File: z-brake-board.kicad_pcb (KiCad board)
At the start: 2 copper layers, 58 x 41 mm, 18 parts, among them J1 to Control Cabinet, J2 to Z Servo, Q2 BTS4142N, U1 LTV-817S, U2 LTV-817S, U3 LTV-817S

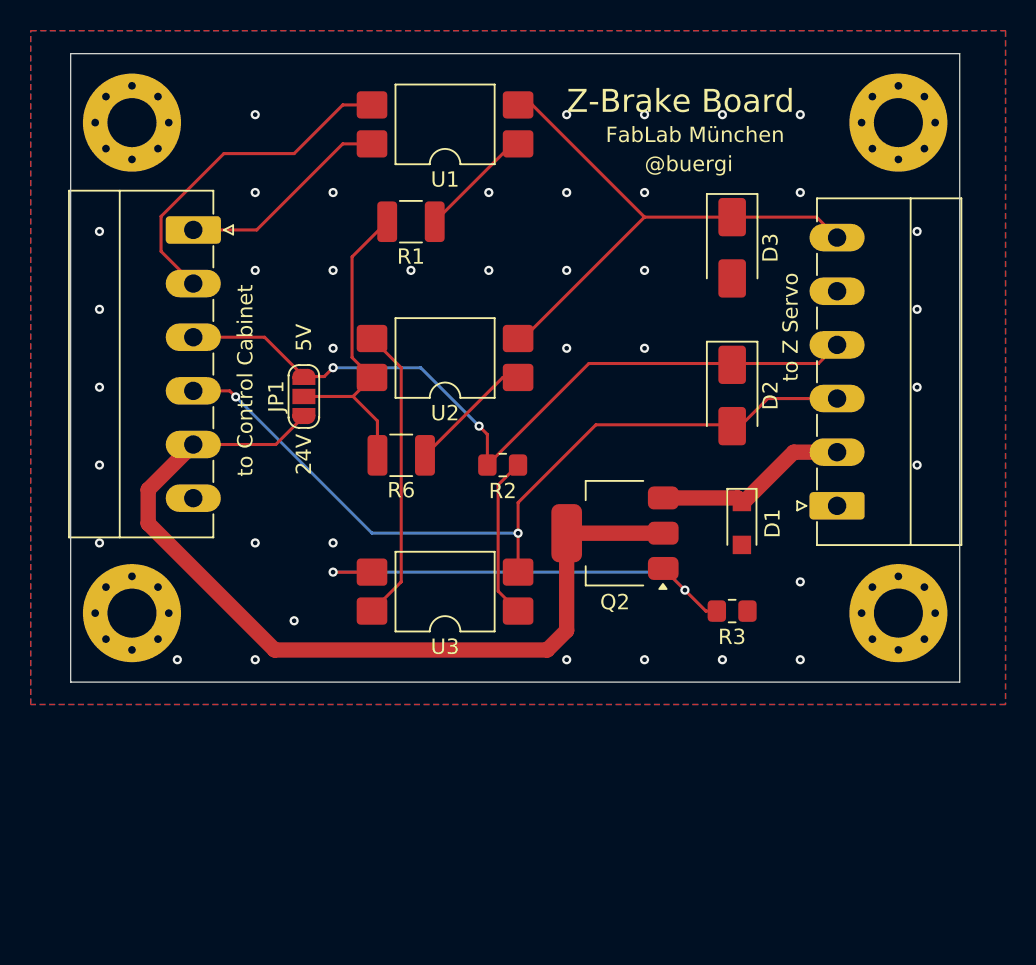
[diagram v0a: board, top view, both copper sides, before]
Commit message: Reworked design (less fancy)
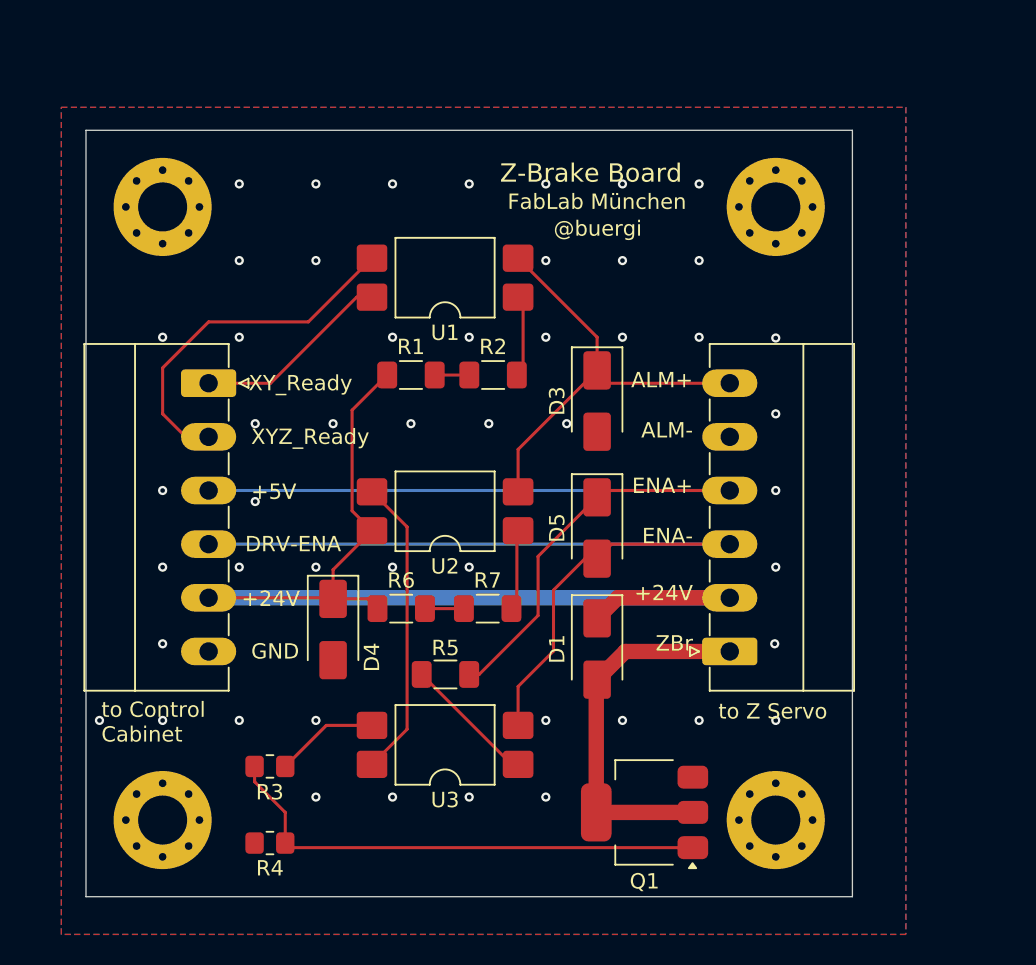
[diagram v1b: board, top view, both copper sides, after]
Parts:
- removed D2: SMAJ24A, Diode_SMD:D_SMA
- removed JP1: VCC Select, Jumper:SolderJumper-3_P1.3mm_Open_RoundedPad1.0x1.5mm_NumberLabels
- removed Q2: BTS4142N, Package_TO_SOT_SMD:SOT-223
- added D4: SMAJ24A, Diode_SMD:D_SMA, F.Cu at (71.1, 64.1)
- added D5: SMAJ5.0A, Diode_SMD:D_SMA, F.Cu at (88.3, 57.4)
- added Q1: IRFL024NPBF, Package_TO_SOT_SMD:SOT-223-3_TabPin2, F.Cu at (91.4, 76.0)
- added R4: 10k, Resistor_SMD:R_0805_2012Metric_Pad1.20x1.40mm_HandSolder, F.Cu at (67.0, 78.0)
- added R5: 2.2k, Resistor_SMD:R_1206_3216Metric_Pad1.30x1.75mm_HandSolder, F.Cu at (78.5, 67.0)
- added R7: 1k, Resistor_SMD:R_1206_3216Metric_Pad1.30x1.75mm_HandSolder, F.Cu at (81.2, 62.7)
- D1: value PMEG6020ER -> US1M; footprint Diode_SMD:Nexperia_CFP3_SOD-123W -> Diode_SMD:D_SMA
- J1: value to Control Cabinet -> Phoenix_MC_1,5_6-G-3.5
- J2: value to Z Servo -> Phoenix_MC_1,5_6-G-3.5
- R1, R6: footprint Resistor_SMD:R_1210_3225Metric_Pad1.30x2.65mm_HandSolder -> Resistor_SMD:R_1206_3216Metric_Pad1.30x1.75mm_HandSolder
- R2: value 220 -> 1k; footprint Resistor_SMD:R_0805_2012Metric_Pad1.20x1.40mm_HandSolder -> Resistor_SMD:R_1206_3216Metric_Pad1.30x1.75mm_HandSolder
- moved R3 31.8 mm to (67.0, 73.0)
- moved H4 15.7 mm to (100.0, 76.5)
- moved H3 13.6 mm to (60.0, 76.5)
- moved D3 13.3 mm to (88.3, 49.2)
- moved D1 12.5 mm to (88.3, 65.3)
- moved J2 11.8 mm to (97.0, 65.5)
- moved J1 10.0 mm to (63.0, 48.0)
- moved U1 10.0 mm to (78.4, 41.1)
- moved R1 10.0 mm to (76.2, 47.5)
- moved R6 10.0 mm to (75.6, 62.7)
- moved U2 10.0 mm to (78.4, 56.4)
- moved U3 10.0 mm to (78.4, 71.6)
- moved H2 9.71 mm to (100.0, 36.5)
- moved R2 5.91 mm to (81.6, 47.5)
- moved H1 5.85 mm to (60.0, 36.5)
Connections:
- D1 pad 1: /~{ZBrake} -> +24V
- D1 pad 2: GND -> /~{ZBrake}
- J1 pad 3: +5V -> /+5V
- J2 pad 1: GND -> /~{ZBrake}
- J2 pad 2: /~{ZBrake} -> +24V
- J2 pad 4: +5V -> /+5V
- R1 pad 1: VCC -> +24V
- R2 pad 1: +5V -> Net-(R1-Pad2)
- R3 pad 1: Net-(Q2-G) -> Net-(Q1-G)
- R3 pad 2: GND -> Net-(R3-Pad2)
- R6 pad 1: VCC -> +24V
- U1 pad 1: Net-(R1-Pad2) -> Net-(R2-Pad2)
- U2 pad 1: Net-(R6-Pad2) -> Net-(R7-Pad2)
- U2 pad 4: VCC -> +24V
- U3 pad 1: Net-(R2-Pad2) -> Net-(R5-Pad2)
- U3 pad 3: Net-(Q2-G) -> Net-(R3-Pad2)
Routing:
- net /+5V: track 0.00 -> 58.4 mm
- net +5V: track 50.3 -> 0.00 mm, vias 2 -> 0
- net Net-(Q1-G): track 0.00 -> 32.5 mm
- net Net-(Q2-G): track 30.6 -> 0.00 mm, vias 2 -> 0
- net VCC: track 21.1 -> 0.00 mm
- net +24V: track 58.3 -> 71.7 mm
- net /~{ZBrake}: track 12.8 -> 24.4 mm
- net Net-(R5-Pad2): track 0.00 -> 8.72 mm
- net /ALM+: track 35.9 -> 28.5 mm
- net Net-(R3-Pad2): track 0.00 -> 6.77 mm
- net Net-(R6-Pad2): track 8.18 -> 2.54 mm
- net Net-(R2-Pad2): track 10.6 -> 5.22 mm
- net Net-(R1-Pad2): track 7.54 -> 2.26 mm
- net Net-(R7-Pad2): track 0.00 -> 5.11 mm
- net /DRV-ENA-5V: track 53.2 -> 57.3 mm, vias 2 -> 0
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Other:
- board size 58 x 41 mm -> 50 x 50 mm
- board text added: "+24V"
- board text added: "+5V"
- board text added: "ALM+"
- board text added: "ALM-"
- board text added: "DRV-ENA"
- board text added: "ENA+"
- board text added: "ENA-"
- board text added: "GND"
- board text added: "XYZ_Ready"
- board text added: "XY_Ready"
- board text added: "ZBr"

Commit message: Shrunk board to 48x48mm
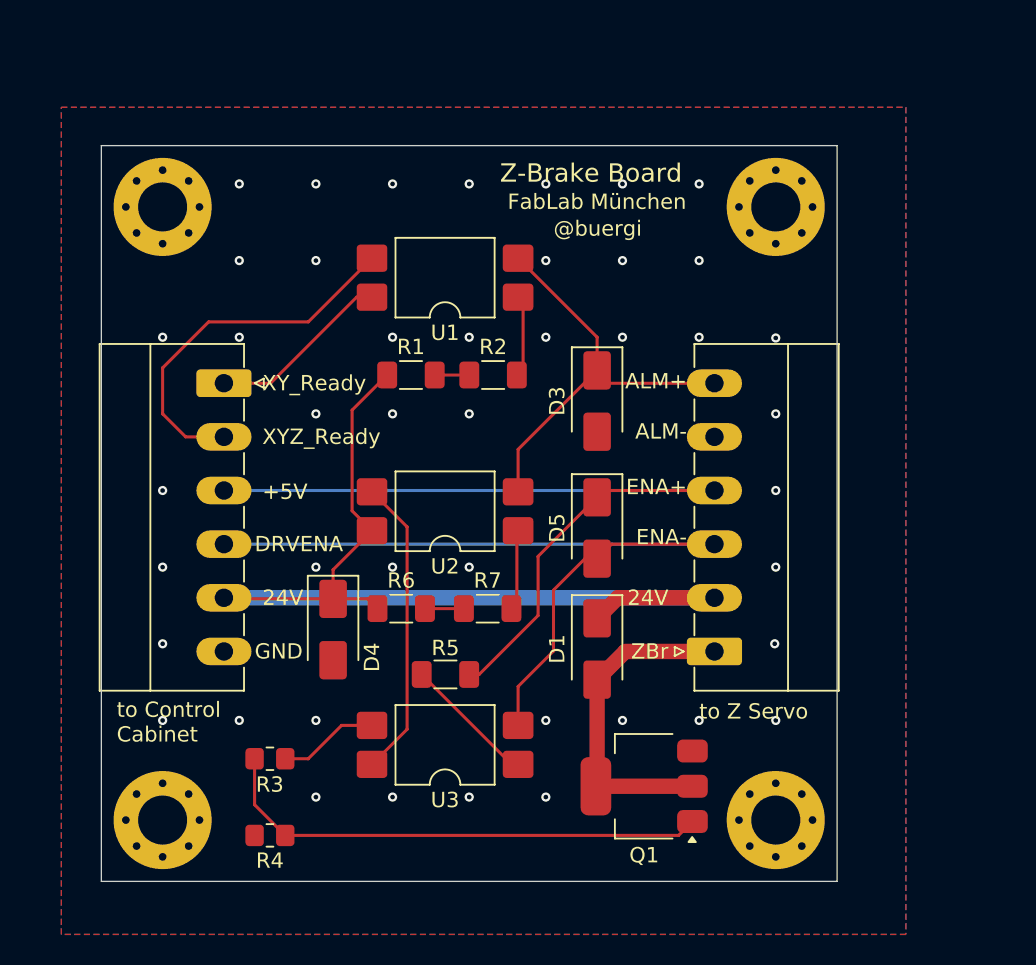
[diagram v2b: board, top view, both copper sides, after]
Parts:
- moved Q1 1.71 mm to (91.4, 74.3)
- moved J1 1.00 mm to (64.0, 48.0)
- moved J2 1.00 mm to (96.0, 65.5)
- moved R3 0.50 mm to (67.0, 72.5)
- moved R4 0.50 mm to (67.0, 77.5)
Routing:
- net /DRV-ENA-5V: track 57.3 -> 53.5 mm
- net +24V: track 71.7 -> 68.4 mm
- net /+5V: track 58.4 -> 55.2 mm
- net /~{ZBrake}: track 24.4 -> 21.8 mm
- net /XY_READY: track 13.0 -> 12.0 mm
- net /XYZ_READY: track 23.2 -> 24.2 mm
- net /ALM+: track 28.5 -> 27.5 mm
- net GND: vias 49 -> 44
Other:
- board size 50 x 50 mm -> 48 x 48 mm
- board text added: "24V"
- board text added: "DRVENA"
- board text removed: "+24V"
- board text removed: "DRV-ENA"

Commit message: U2 removed
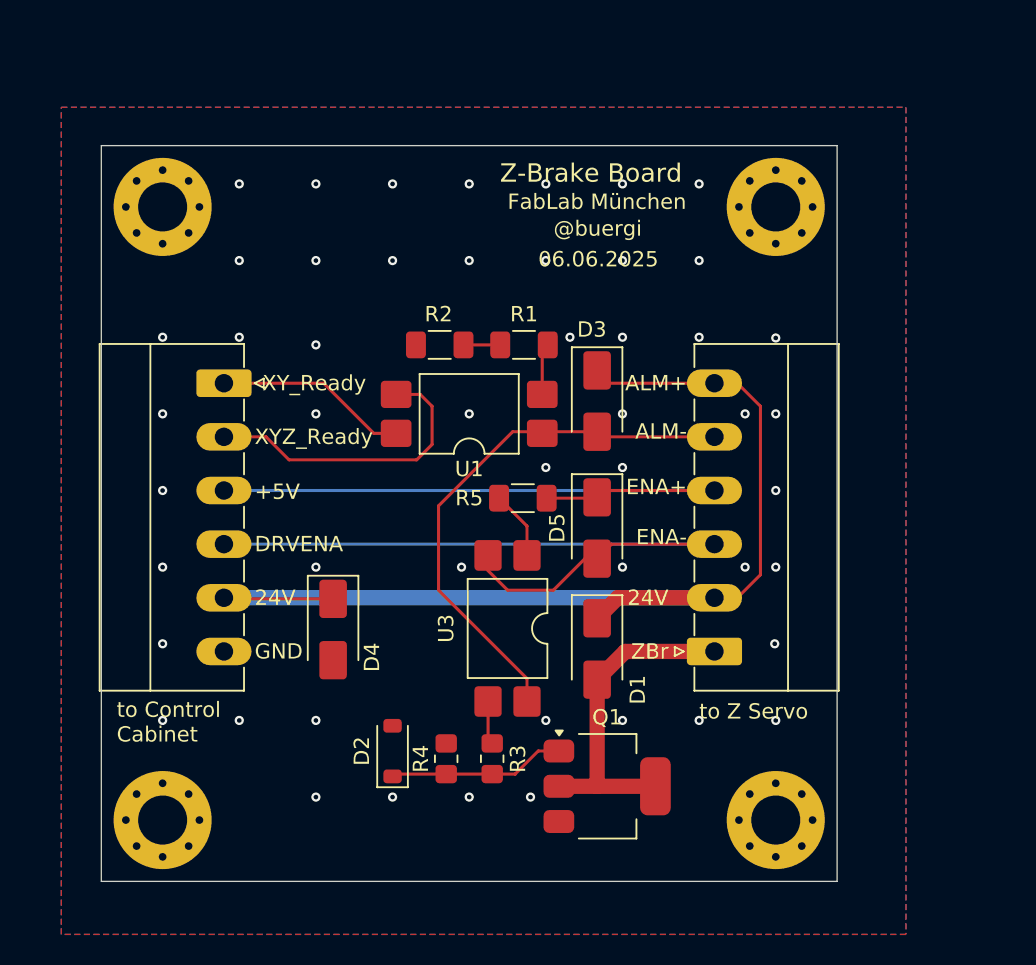
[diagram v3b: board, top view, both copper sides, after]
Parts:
- removed R6, R7: 1k, Resistor_SMD:R_1206_3216Metric_Pad1.30x1.75mm_HandSolder
- removed U2: LTV-817S, Package_DIP:SMDIP-4_W9.53mm
- added D2: 12V, Diode_SMD:D_SOD-123, F.Cu at (75.0, 72.0)
- moved R3 14.5 mm to (81.5, 72.5), turned to 90 degrees
- moved R5 12.6 mm to (83.5, 55.5)
- moved R4 12.5 mm to (78.5, 72.5), turned to 90 degrees
- moved U1 9.02 mm to (80.0, 50.0)
- moved U3 8.62 mm to (82.5, 64.0), turned to -90 degrees
- moved R1 7.63 mm to (83.6, 45.5), turned to 180 degrees
- moved R2 4.00 mm to (78.1, 45.5), turned to 180 degrees
- moved Q1 2.42 mm to (89.0, 74.3), turned to 0 degrees
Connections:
- net /XYZ_READY renamed Net-(J1-Pin_2)
- D3 pad 1: /ALM+ -> +24V
- D3 pad 2: GND -> /ALM-
- J2 pad 5: GND -> /ALM-
- J2 pad 6: /ALM+ -> +24V
- R1 pad 1: +24V -> Net-(R1-Pad1)
- R2 pad 2: Net-(R2-Pad2) -> GND
- U1 pad 1: Net-(R2-Pad2) -> /ALM-
- U1 pad 2: /ALM+ -> Net-(R1-Pad1)
- U3 pad 4: Net-(U2-Pad3) -> /ALM-
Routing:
- net /ALM-: track 0.00 -> 36.4 mm
- net /ALM+: track 27.5 -> 0.00 mm
- net Net-(D2-K): track 32.8 -> 11.5 mm
- net Net-(U2-Pad3): track 19.7 -> 0.00 mm
- net /+5V: track 55.2 -> 42.5 mm
- net +24V: track 68.4 -> 74.3 mm
- net Net-(R2-Pad2): track 5.22 -> 0.00 mm
- net Net-(R7-Pad2): track 5.11 -> 0.00 mm
- net Net-(R5-Pad2): track 8.72 -> 4.49 mm
- net /DRV-ENA-5V: track 53.5 -> 49.5 mm
- net Net-(R1-Pad1): track 0.00 -> 3.92 mm
- net Net-(J1-Pin_2): track 24.2 -> 20.3 mm
- net Net-(R3-Pad2): track 6.56 -> 2.85 mm
- net Net-(R6-Pad2): track 2.54 -> 0.00 mm
- net /XY_READY: track 12.0 -> 12.6 mm
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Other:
- board text added: "06.06.2025"

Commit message: Minor cleanups
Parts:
- removed U3: LTV-817S, Package_DIP:SMDIP-4_W9.53mm
- added U2: LTV-817S, Package_DIP:SMDIP-4_W9.53mm, F.Cu at (80.0, 61.2)
- moved D2 4.67 mm to (76.2, 67.5)
- moved R4 4.67 mm to (79.8, 68.0)
- moved R3 4.61 mm to (82.5, 68.0)
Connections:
- net Net-(J1-Pin_2) renamed /XYZ_READY
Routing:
- net Net-(R3-Pad2): track 2.85 -> 10.2 mm
- net /DRV-ENA-5V: track 49.5 -> 43.8 mm
- net /ALM-: track 36.4 -> 31.8 mm
- net Net-(R5-Pad2): track 4.49 -> 8.17 mm
- net Net-(D2-K): track 11.5 -> 13.7 mm
- net GND: vias 50 -> 51
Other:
- board text added: "DRV-ENA"
- board text removed: "DRVENA"
